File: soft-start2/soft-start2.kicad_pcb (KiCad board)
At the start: 2 copper layers, 27 parts, among them J3 Conn_01x01_Pin, J4 Conn_01x01_Pin, Q1 IRFB3004PbF, Q2 IRFB3004PbF, U1 TLC555xD, U2 IRS10752LPbF

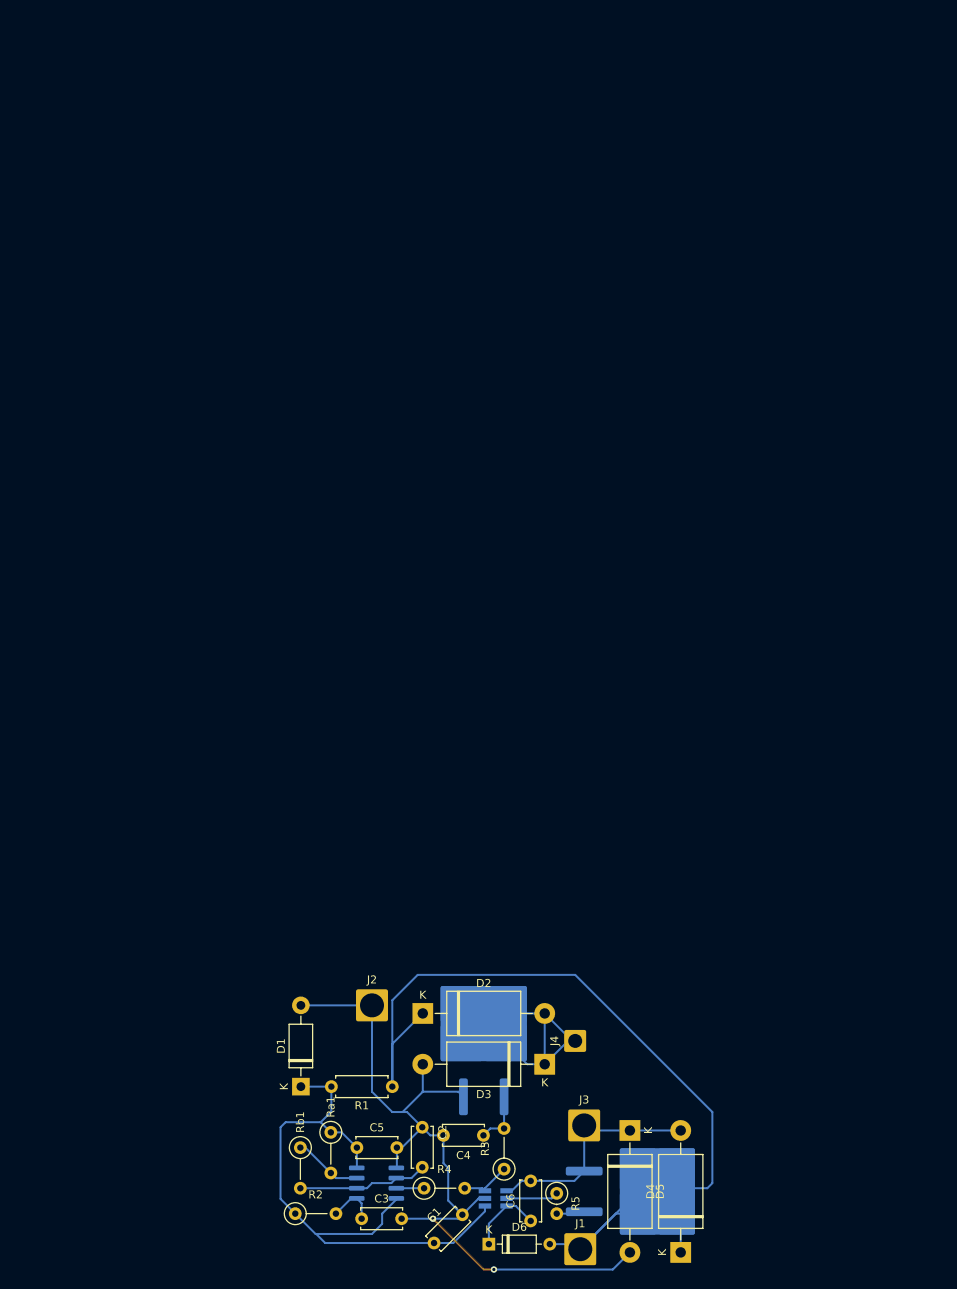
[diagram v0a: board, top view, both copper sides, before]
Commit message: [soft-start] Add calculus file. Add integrating and comparator schematic for turning on full-power.
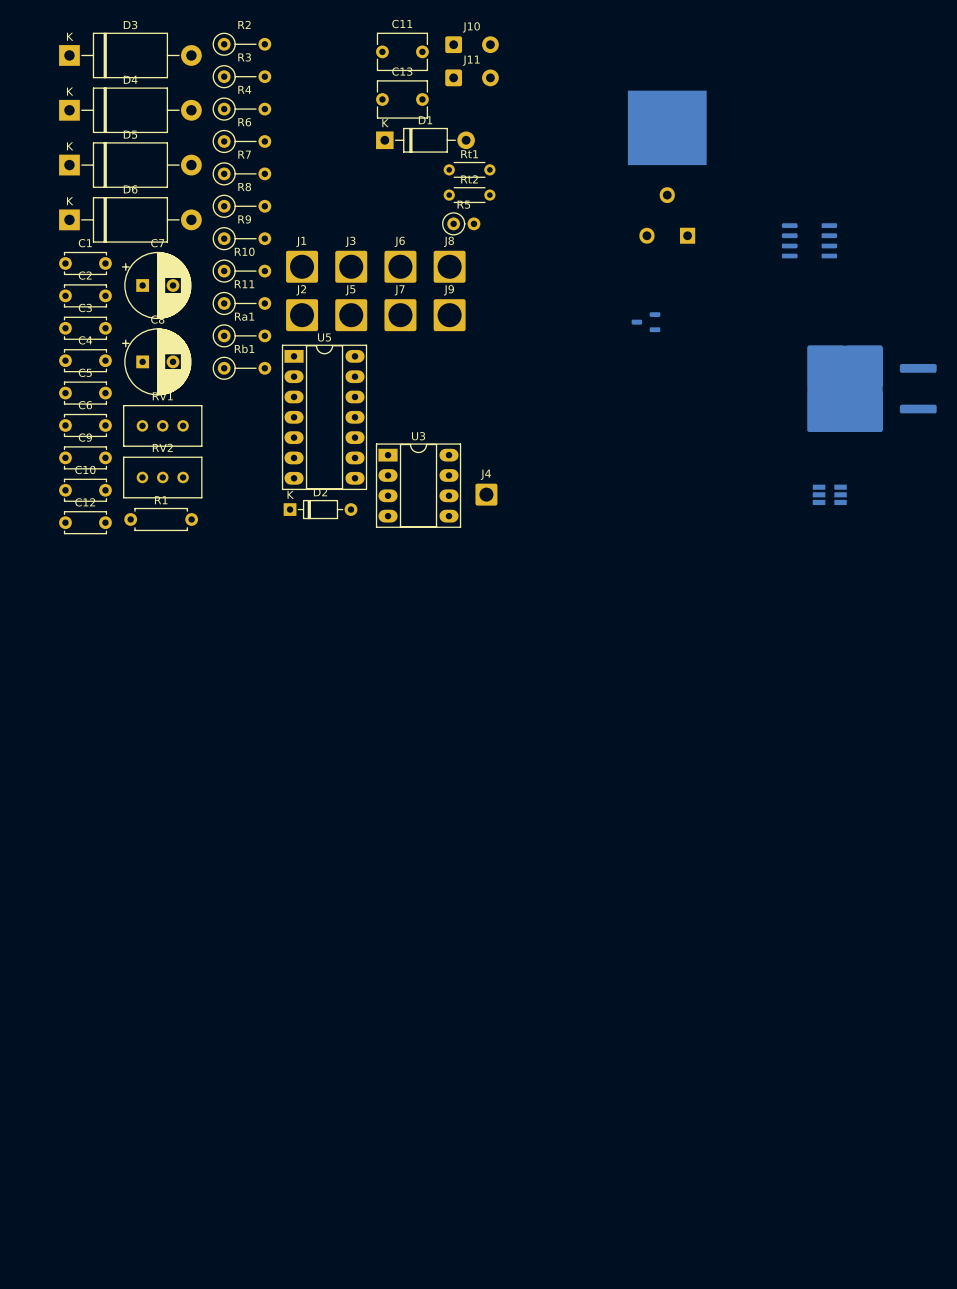
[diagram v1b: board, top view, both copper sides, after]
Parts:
- added C10: 22nF, Capacitor_THT:C_Disc_D5.0mm_W2.5mm_P5.00mm, F.Cu at (23.9, 74.7)
- added C11: 22nF, Capacitor_THT:C_Disc_D6.0mm_W4.4mm_P5.00mm, F.Cu at (63.5, 19.9)
- added C12: 0.22uF, Capacitor_THT:C_Disc_D5.0mm_W2.5mm_P5.00mm, F.Cu at (23.9, 78.7)
- added C13: 22nF, Capacitor_THT:C_Disc_D6.0mm_W4.4mm_P5.00mm, F.Cu at (63.5, 25.8)
- added C7: 470uF, Capacitor_THT:CP_Radial_D8.0mm_P3.80mm, F.Cu at (33.6, 49.1)
- added C8: 470uF, Capacitor_THT:CP_Radial_D8.0mm_P3.80mm, F.Cu at (33.6, 58.6)
- added C9: C, Capacitor_THT:C_Disc_D5.0mm_W2.5mm_P5.00mm, F.Cu at (23.9, 70.6)
- added J10: Conn_01x02_Pin, Connector_Wire:SolderWire-0.5sqmm_1x02_P4.6mm_D0.9mm_OD2.1mm, F.Cu at (72.4, 19.0)
- added J11: Conn_01x02_Socket, Connector_Wire:SolderWire-0.5sqmm_1x02_P4.6mm_D0.9mm_OD2.1mm, F.Cu at (72.4, 23.1)
- added J5: Conn_01x01_Pin, Connector_Wire:SolderWire-2.5sqmm_1x01_D2.4mm_OD3.6mm, F.Cu at (59.6, 52.8)
- added J6: ~, Connector_Wire:SolderWire-2.5sqmm_1x01_D2.4mm_OD3.6mm, F.Cu at (65.8, 46.7)
- added J7: ~, Connector_Wire:SolderWire-2.5sqmm_1x01_D2.4mm_OD3.6mm, F.Cu at (65.8, 52.8)
- added J8: Conn_01x01_Pin, Connector_Wire:SolderWire-2.5sqmm_1x01_D2.4mm_OD3.6mm, F.Cu at (71.9, 46.7)
- added J9: ~, Connector_Wire:SolderWire-2.5sqmm_1x01_D2.4mm_OD3.6mm, F.Cu at (71.9, 52.8)
- added R10: 100k, Resistor_THT:R_Axial_DIN0207_L6.3mm_D2.5mm_P5.08mm_Vertical, F.Cu at (43.8, 47.3)
- added R11: 100k, Resistor_THT:R_Axial_DIN0207_L6.3mm_D2.5mm_P5.08mm_Vertical, F.Cu at (43.8, 51.3)
- added R6: 5.1k, Resistor_THT:R_Axial_DIN0207_L6.3mm_D2.5mm_P5.08mm_Vertical, F.Cu at (43.8, 31.1)
- added R7: 160k, Resistor_THT:R_Axial_DIN0207_L6.3mm_D2.5mm_P5.08mm_Vertical, F.Cu at (43.8, 35.1)
- added R8: 220k, Resistor_THT:R_Axial_DIN0207_L6.3mm_D2.5mm_P5.08mm_Vertical, F.Cu at (43.8, 39.2)
- added R9: 100k, Resistor_THT:R_Axial_DIN0207_L6.3mm_D2.5mm_P5.08mm_Vertical, F.Cu at (43.8, 43.2)
- added RV1: 2.2k, Potentiometer_THT:Potentiometer_Bourns_3296W_Vertical, F.Cu at (38.6, 66.6)
- added RV2: 1M, Potentiometer_THT:Potentiometer_Bourns_3296W_Vertical, F.Cu at (38.6, 73.1)
- added Rt1: 5.1k, Resistor_THT:R_Axial_DIN0204_L3.6mm_D1.6mm_P5.08mm_Horizontal, F.Cu at (71.9, 34.6)
- added Rt2: 5.1k, Resistor_THT:R_Axial_DIN0204_L3.6mm_D1.6mm_P5.08mm_Horizontal, F.Cu at (71.9, 37.8)
- added U3: LM393, Package_DIP:DIP-8_W7.62mm_Socket_LongPads, F.Cu at (64.2, 70.3)
- added U4: IRS10752LPbF, Package_TO_SOT_SMD:SOT-23-6_Handsoldering, B.Cu at (119.5, 75.2)
- added U5: 4011, Package_DIP:DIP-14_W7.62mm_Socket_LongPads, F.Cu at (52.5, 57.9)
- C6: value C -> 0.1uF
- D2: value 1.5KExxA -> 1N4148; footprint Diode_THT:D_DO-201AE_P15.24mm_Horizontal -> Diode_THT:D_DO-35_SOD27_P7.62mm_Horizontal
- D6: value 1N4148 -> 1.5KExxA; footprint Diode_THT:D_DO-35_SOD27_P7.62mm_Horizontal -> Diode_THT:D_DO-201AE_P15.24mm_Horizontal
- Q1: footprint Package_TO_SOT_SMD:TO-263-2 -> LIB:TO-220-3-4_Horizontal_TabDown
- R3, Rb1: value R -> 1k
- R4: value 1k -> 200
- Ra1: value R -> 10k
- U1: value TLC555xD -> ~; footprint Package_SO:SOIC-8_3.9x4.9mm_P1.27mm -> Package_TO_SOT_SMD:SOT-23-3
- U2: value IRS10752LPbF -> TLC555xD; footprint Package_TO_SOT_SMD:SOT-23-6_Handsoldering -> Package_SO:SOIC-8_3.9x4.9mm_P1.27mm
- moved D4 161.9 mm to (24.4, 27.2), turned to 0 degrees
- moved R2 146.4 mm to (43.8, 18.9)
- moved R3 141.0 mm to (43.8, 23.0), turned to 0 degrees
- moved D5 139.5 mm to (24.4, 34.0), turned to 0 degrees
- moved D3 139.4 mm to (24.4, 20.3), turned to 0 degrees
- moved D6 138.3 mm to (24.4, 40.9)
- moved R4 137.2 mm to (43.8, 27.0)
- moved C1 130.8 mm to (23.9, 46.3), turned to 0 degrees
- moved J1 127.6 mm to (53.5, 46.7)
- moved U2 126.0 mm to (116.9, 43.5), turned to 180 degrees
- moved R5 121.9 mm to (72.4, 41.4), turned to 0 degrees
- moved D1 118.8 mm to (63.8, 30.9), turned to 0 degrees
- moved C2 117.7 mm to (23.9, 50.4), turned to 0 degrees
- moved C3 117.3 mm to (23.9, 54.4)
- moved C6 115.2 mm to (23.9, 66.6), turned to 0 degrees
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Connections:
- C1 pad 1: VCC -> +BATT
- C2 pad 1: /U1_TRIG -> VCC
- C3 pad 1: /U1_CONT -> VCC
- C4 pad 1: Net-(Q1-G) -> VCC
- C4 pad 2: GND -> GND2
- C5 pad 2: GND -> GND2
- C6 pad 1: Net-(D6-K) -> /U1_TRIG
- C6 pad 2: /POWER_OUTPUT -> GND
- D2 pad 1: +BATT -> Net-(D2-K)
- D2 pad 2: Net-(D2-A2) -> +BATT
- D3 pad 1: Net-(D2-A2) -> +BATT
- D3 pad 2: GND -> /POWER_OUTPUT
- D4 pad 1: +BATT -> /POWER_OUTPUT
- D4 pad 2: /POWER_OUTPUT -> GND
- D5 pad 1: /POWER_OUTPUT -> +BATT2
- D5 pad 2: GND -> Net-(D5-A2)
- D6 pad 1: Net-(D6-K) -> Net-(D5-A2)
- D6 pad 2: +BATT -> GND2
- J4 pad 1: Net-(D2-A2) -> Net-(D5-A2)
- Q1 pad 2: Net-(D2-A2) -> +BATT
- Q1 pad 3: GND -> /POWER_OUTPUT
- Q2 pad 1: Net-(Q2-G) -> /TRIGGER_OUT
- Q2 pad 2: +BATT -> Net-(D5-A2)
- Q2 pad 3: /POWER_OUTPUT -> GND2
- R2 pad 2: /U1_CONT -> Net-(U1-G)
- R3 pad 1: /POWER_CONTROL -> Net-(U2-Q)
- R3 pad 2: Net-(Q1-G) -> /PWM
- R4 pad 1: Net-(U1-Q) -> Net-(U1-K)
- R4 pad 2: /POWER_CONTROL -> Net-(R4-Pad2)
- R5 pad 1: Net-(U2-HO) -> Net-(U4-HO)
- R5 pad 2: Net-(Q2-G) -> Net-(Q1-G)
- U1 pad 1: GND -> Net-(U1-K)
- U1 pad 2: /U1_TRIG -> Net-(U1-G)
- U1 pad 3: Net-(U1-Q) -> VCC
- U2 pad 1: VCC -> GND
- U2 pad 2: GND -> /U1_TRIG
- U2 pad 3: /POWER_CONTROL -> Net-(U2-Q)
- U2 pad 4: /POWER_OUTPUT -> VCC
- U2 pad 5: Net-(U2-HO) -> /U1_CONT
- U2 pad 6: Net-(D6-K) -> /U1_TRIG
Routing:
- net +BATT: track 120.7 -> 0.00 mm
- net GND: track 100.5 -> 0.00 mm, vias 2 -> 0
- net VCC: track 74.3 -> 0.00 mm
- net Net-(D2-A2): track 30.7 -> 0.00 mm
- net /POWER_OUTPUT: track 28.8 -> 0.00 mm
- net /U1_TRIG: track 16.3 -> 0.00 mm
- net Net-(D6-K): track 9.47 -> 0.00 mm
- net /U1_DISCH: track 8.63 -> 0.00 mm
- net Net-(Q1-G): track 6.90 -> 0.00 mm
- net Net-(U2-HO): track 6.85 -> 0.00 mm
- net /POWER_CONTROL: track 6.36 -> 0.00 mm
- net /U1_CONT: track 6.19 -> 0.00 mm
- net Net-(Q2-G): track 3.53 -> 0.00 mm
- net Net-(U1-Q): track 3.46 -> 0.00 mm

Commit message: [soft-start] Change comparator. Start PCB.
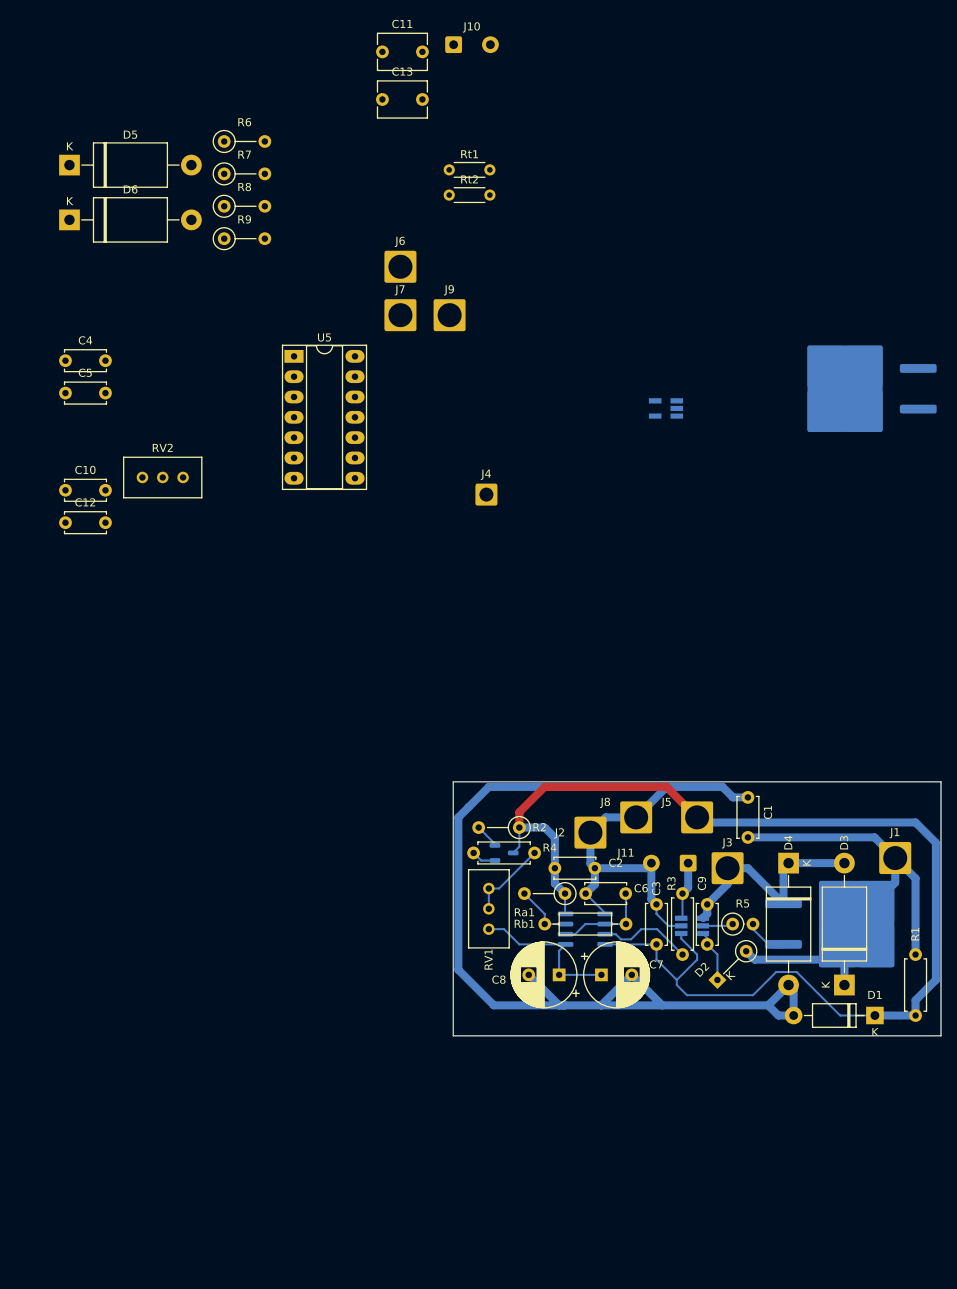
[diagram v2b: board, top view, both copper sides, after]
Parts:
- removed R10, R11: 100k, Resistor_THT:R_Axial_DIN0207_L6.3mm_D2.5mm_P5.08mm_Vertical
- D2: footprint Diode_THT:D_DO-35_SOD27_P7.62mm_Horizontal -> Diode_THT:D_DO-35_SOD27_P5.08mm_Vertical_KathodeUp
- Q1: footprint LIB:TO-220-3-4_Horizontal_TabDown -> Package_TO_SOT_SMD:TO-263-2
- R3, R4: footprint Resistor_THT:R_Axial_DIN0207_L6.3mm_D2.5mm_P5.08mm_Vertical -> Resistor_THT:R_Axial_DIN0207_L6.3mm_D2.5mm_P7.62mm_Horizontal
- Rb1: footprint Resistor_THT:R_Axial_DIN0207_L6.3mm_D2.5mm_P5.08mm_Vertical -> Resistor_THT:R_Axial_DIN0207_L6.3mm_D2.5mm_P10.16mm_Horizontal
- U1: value ~ -> P0102BL
- U3: value LM393 -> TS391ILT; footprint Package_DIP:DIP-8_W7.62mm_Socket_LongPads -> Package_TO_SOT_SMD:SOT-23-5_HandSoldering; moved to B.Cu
- moved D3 151.3 mm to (121.3, 136.5), turned to 90 degrees
- moved D4 130.1 mm to (114.3, 121.3), turned to -90 degrees
- moved D1 125.4 mm to (125.1, 140.3), turned to 180 degrees
- moved R3 123.8 mm to (101.0, 132.7), turned to 90 degrees
- moved R1 112.2 mm to (130.2, 132.7), turned to -90 degrees
- moved C1 111.5 mm to (109.2, 118.1), turned to 90 degrees
- moved C3 106.7 mm to (97.8, 131.4), turned to 90 degrees
- moved J1 104.7 mm to (127.6, 120.7)
- moved R2 104.6 mm to (80.6, 116.8), turned to 180 degrees
- moved C7 103.5 mm to (90.9, 135.3)
- moved J11 102.4 mm to (101.8, 121.3), turned to 180 degrees
- moved C9 100.7 mm to (104.1, 131.4), turned to 90 degrees
- moved R4 98.1 mm to (74.9, 120.0)
- moved R5 94.2 mm to (107.3, 128.9)
- moved C2 94.1 mm to (85.1, 121.9)
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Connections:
- C4 pad 1: VCC -> VCC2
- C5 pad 1: VCC -> VCC2
- U3 pad 1: Net-(U3A--) -> Net-(C10-Pad1)
- U3 pad 2: Net-(U3A--) -> GND2
- U3 pad 3: Net-(U3A-+) -> /INT_REF
- U3 pad 4: unconnected-(U3C-V--Pad4) -> /INT
- U3 pad 5: /INT -> VCC2
- U5 pad 7: unconnected-(U5E-VSS-Pad7) -> GND2
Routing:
- net GND: track 0.00 -> 168.9 mm
- net VCC: track 0.00 -> 153.4 mm
- net +BATT: track 0.00 -> 56.8 mm
- net /POWER_OUTPUT: track 0.00 -> 28.7 mm
- net /U1_CONT: track 0.00 -> 19.8 mm
- net /U1_TRIG: track 0.00 -> 11.9 mm
- net Net-(U2-Q): track 0.00 -> 11.8 mm
- net Net-(R4-Pad2): track 0.00 -> 10.1 mm
- net /U1_DISCH: track 0.00 -> 7.47 mm
- net /PWM: track 0.00 -> 7.26 mm
- net Net-(D2-K): track 0.00 -> 6.57 mm
- net Net-(Q1-G): track 0.00 -> 6.50 mm
- net Net-(U4-HO): track 0.00 -> 3.82 mm
- net Net-(U1-G): track 0.00 -> 3.07 mm
- net Net-(U1-K): track 0.00 -> 3.07 mm
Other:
- board outline added: 61 x 31.8 mm

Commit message: [soft-start] Complete basic PCB for PWM soft-start
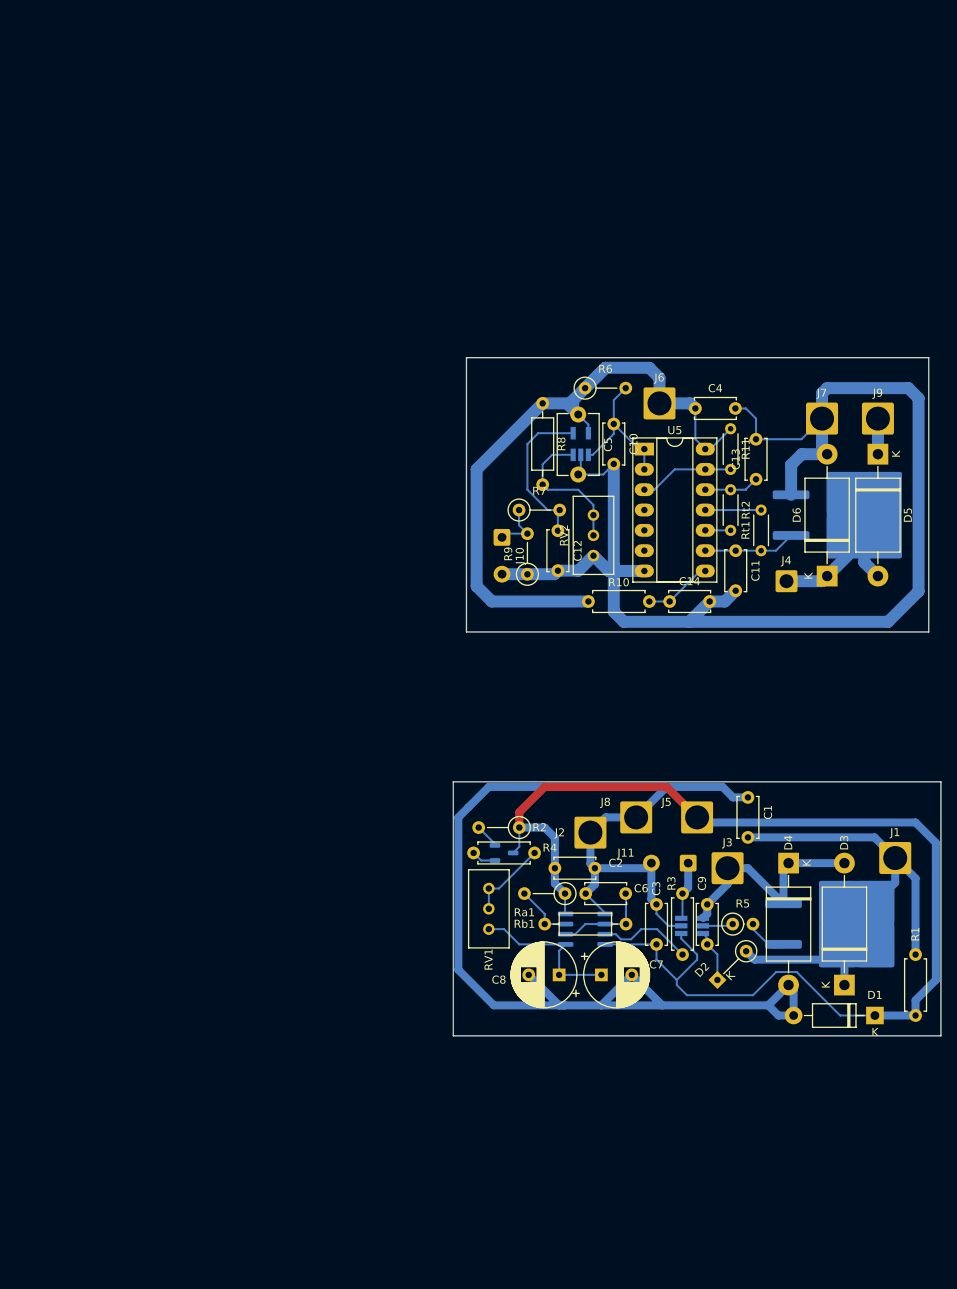
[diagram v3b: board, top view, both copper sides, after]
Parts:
- added C14: 22nF, Capacitor_THT:C_Disc_D5.0mm_W2.5mm_P5.00mm, F.Cu at (99.4, 88.6)
- added R10: 5.1k, Resistor_THT:R_Axial_DIN0207_L6.3mm_D2.5mm_P7.62mm_Horizontal, F.Cu at (89.3, 88.6)
- added R11: 5.1k, Resistor_THT:R_Axial_DIN0204_L3.6mm_D1.6mm_P5.08mm_Horizontal, F.Cu at (107.1, 67.0)
- C11, C13: footprint Capacitor_THT:C_Disc_D6.0mm_W4.4mm_P5.00mm -> Capacitor_THT:C_Disc_D5.0mm_W2.5mm_P5.00mm
- C5: footprint Capacitor_THT:C_Disc_D5.0mm_W2.5mm_P5.00mm -> Capacitor_THT:C_Disc_D7.5mm_W5.0mm_P7.50mm
- R8: footprint Resistor_THT:R_Axial_DIN0207_L6.3mm_D2.5mm_P5.08mm_Vertical -> Resistor_THT:R_Axial_DIN0207_L6.3mm_D2.5mm_P10.16mm_Horizontal
- moved D5 107.3 mm to (125.5, 70.2), turned to -90 degrees
- moved D6 104.7 mm to (119.1, 85.4), turned to 90 degrees
- moved C4 79.0 mm to (102.7, 64.5)
- moved C11 76.4 mm to (107.7, 82.2), turned to -90 degrees
- moved C10 69.0 mm to (92.5, 66.4), turned to -90 degrees
- moved C13 66.6 mm to (110.2, 73.3), turned to 90 degrees
- moved C5 64.1 mm to (88.0, 65.2), turned to -90 degrees
- moved J10 61.9 mm to (78.5, 80.6), turned to -90 degrees
- moved C12 61.6 mm to (85.5, 79.7), turned to -90 degrees
- moved Rt1 61.5 mm to (110.9, 82.2), turned to 90 degrees
- moved R9 56.5 mm to (81.7, 85.2), turned to 90 degrees
- moved R7 55.9 mm to (80.6, 77.2)
- moved J9 55.1 mm to (125.5, 65.7)
- moved R6 54.6 mm to (88.9, 61.9)
- moved J7 54.3 mm to (118.5, 65.7)
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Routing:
- net GND2: track 0.00 -> 162.8 mm
- net VCC2: track 0.00 -> 92.7 mm
- net Net-(D5-A2): track 0.00 -> 23.2 mm
- net /INT: track 0.00 -> 19.8 mm
- net Net-(C10-Pad1): track 0.00 -> 18.3 mm
- net /INT_REF: track 0.00 -> 18.1 mm
- net /TRIGGER_SET: track 0.00 -> 11.8 mm
- net /TRIGGER_OUT: track 0.00 -> 11.5 mm
- net /TRIGGER_RESET: track 0.00 -> 8.58 mm
- net Net-(Rt1-Pad2): track 0.00 -> 6.98 mm
- net Net-(C13-Pad1): track 0.00 -> 6.91 mm
- net /PWM2: track 0.00 -> 6.75 mm
- net +BATT2: track 0.00 -> 4.45 mm
- net Net-(Rt2-Pad2): track 0.00 -> 3.17 mm
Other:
- board size 61 x 31.8 mm -> 61 x 84.8 mm
